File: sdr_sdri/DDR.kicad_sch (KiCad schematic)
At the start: 5 parts

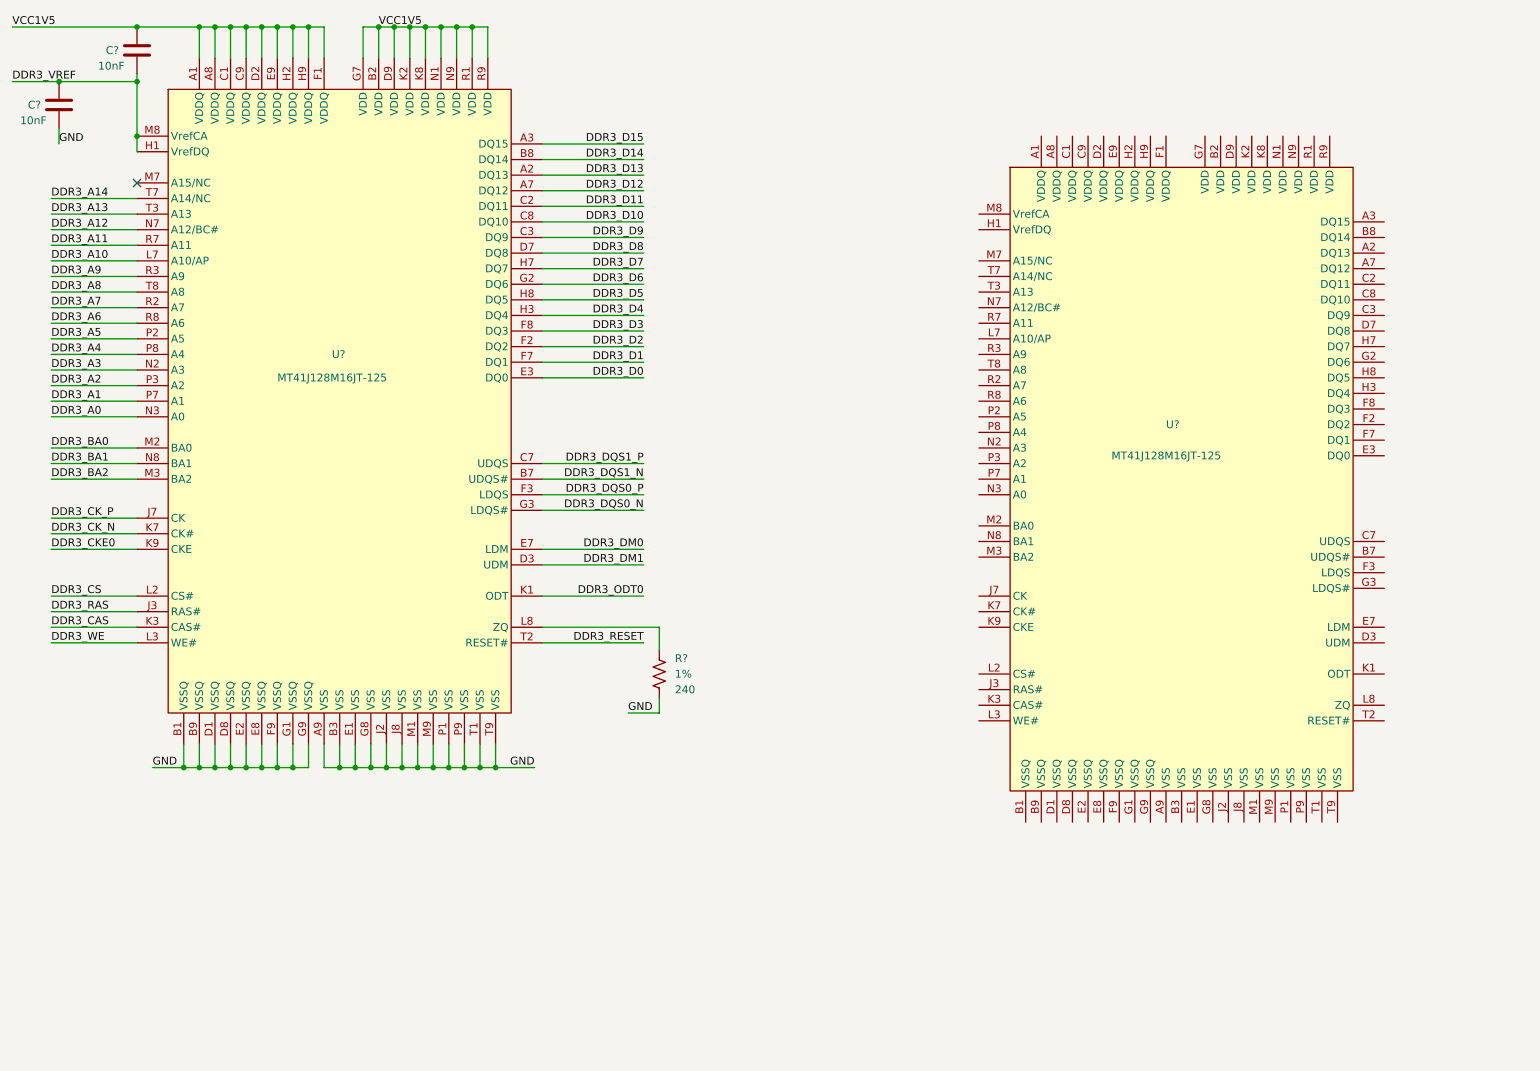
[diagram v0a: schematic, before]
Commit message: add ddr device
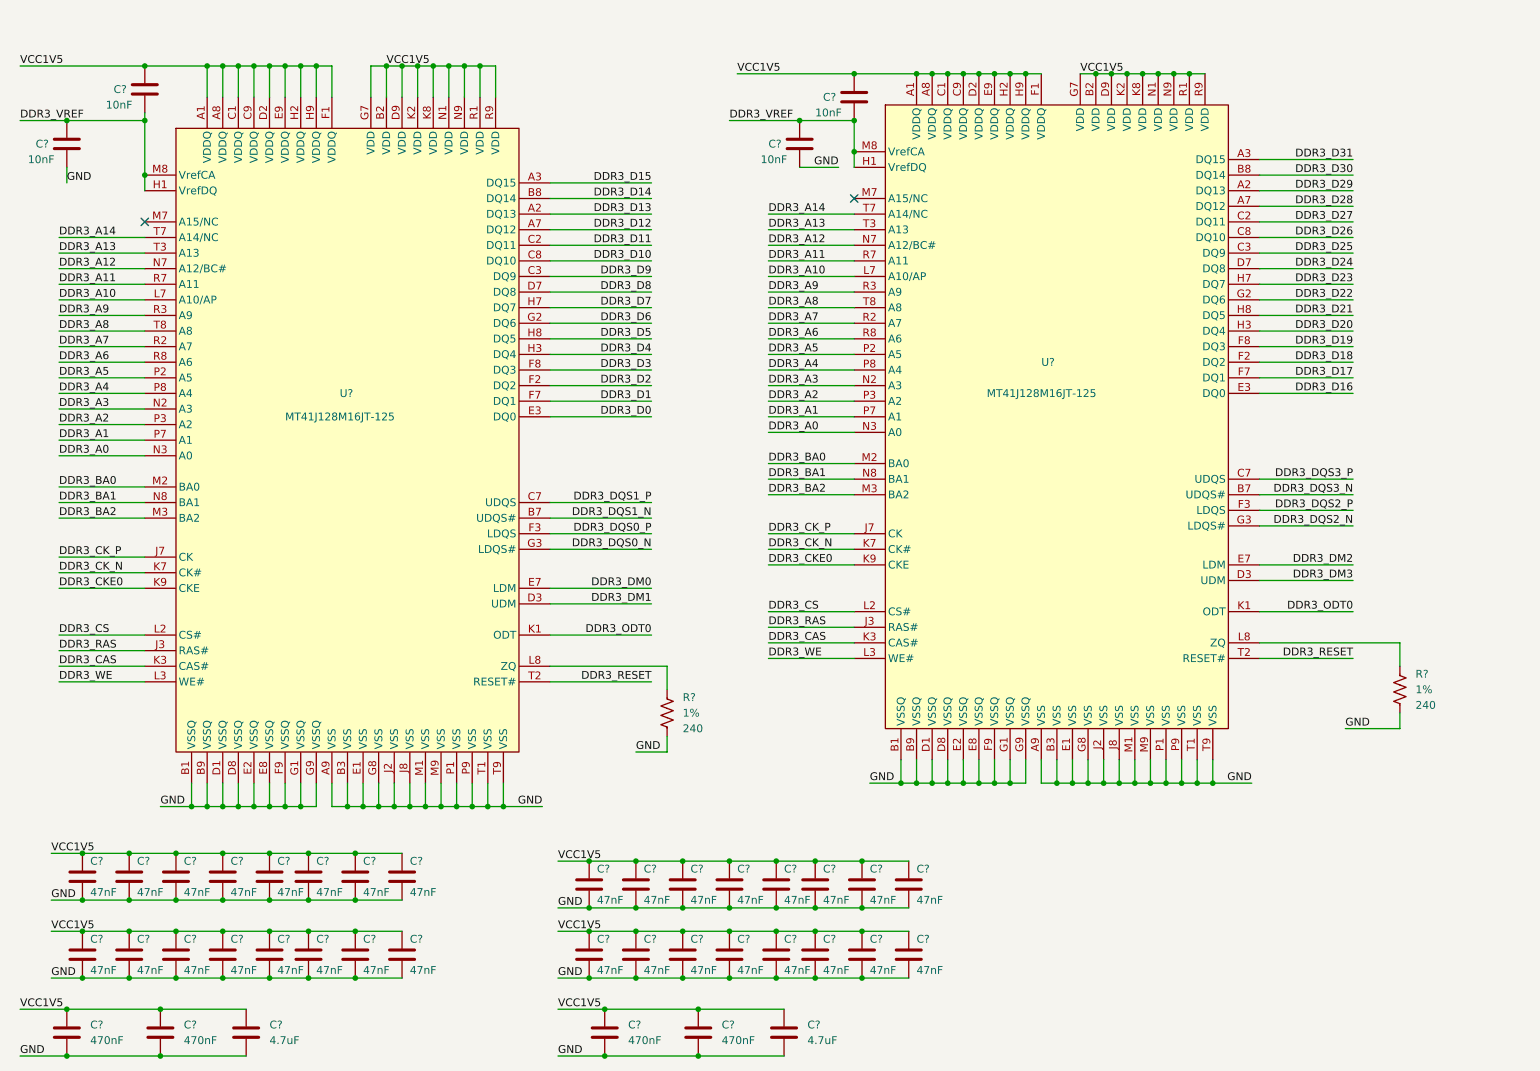
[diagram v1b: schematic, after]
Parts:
- added C? (x32): 47nF, symbol Device:C
- added C? (x2): 4.7uF, symbol Device:C
- added C? (x2): 10nF, symbol Device:C
- added C? (x4): 470nF, symbol Device:C
- added R?: 240, symbol Device:R_US
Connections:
- net DDR3_A0: now also U?.N3 (A0)
- net DDR3_A1: now also U?.P7 (A1)
- net DDR3_A10: now also U?.L7 (A10/AP)
- net DDR3_A11: now also U?.R7 (A11)
- net DDR3_A12: now also U?.N7 (A12/BC#)
- net DDR3_A13: now also U?.T3 (A13)
- net DDR3_A14: now also U?.T7 (A14/NC)
- net DDR3_A2: now also U?.P3 (A2)
- net DDR3_A3: now also U?.N2 (A3)
- net DDR3_A4: now also U?.P8 (A4)
- net DDR3_A5: now also U?.P2 (A5)
- net DDR3_A6: now also U?.R8 (A6)
- net DDR3_A7: now also U?.R2 (A7)
- net DDR3_A8: now also U?.T8 (A8)
- net DDR3_A9: now also U?.R3 (A9)
- net DDR3_BA0: now also U?.M2 (BA0)
- net DDR3_BA1: now also U?.N8 (BA1)
- net DDR3_BA2: now also U?.M3 (BA2)
- net DDR3_CAS: now also U?.K3 (CAS#)
- net DDR3_CKE0: now also U?.K9 (CKE)
- net DDR3_CK_N: now also U?.K7 (CK#)
- net DDR3_CK_P: now also U?.J7 (CK)
- net DDR3_CS: now also U?.L2 (CS#)
- net DDR3_ODT0: now also U?.K1 (ODT)
- net DDR3_RAS: now also U?.J3 (RAS#)
- net DDR3_RESET: now also U?.T2 (RESET#)
- net DDR3_VREF: now also U?.H1 (VrefDQ), U?.M8 (VrefCA), C?.1, C?.2
- net DDR3_WE: now also U?.L3 (WE#)
- net GND: now also U?.A9 (VSS), U?.B1 (VSSQ), U?.B3 (VSS), U?.B9 (VSSQ), U?.D1 (VSSQ), U?.D8 (VSSQ), U?.E1 (VSS), U?.E2 (VSSQ), U?.E8 (VSSQ), U?.F9 (VSSQ), U?.G1 (VSSQ), U?.G8 (VSS), U?.G9 (VSSQ), U?.J2 (VSS), U?.J8 (VSS), U?.M1 (VSS), U?.M9 (VSS), U?.P1 (VSS), U?.P9 (VSS), U?.T1 (VSS), U?.T9 (VSS), C?.2, C?.2, C?.2, C?.2, C?.2, C?.2, C?.2, C?.2, C?.2, C?.2, C?.2, C?.2, C?.2, C?.2, C?.2, C?.2, C?.2, C?.2, C?.2, C?.2, C?.2, C?.2, C?.2, C?.2, C?.2, C?.2, C?.2, C?.2, C?.2, C?.2, C?.2, C?.2, C?.2, C?.2, C?.2, C?.2, C?.2, C?.2, C?.2, R?.2
- net VCC1V5: now also U?.A1 (VDDQ), U?.A8 (VDDQ), U?.B2 (VDD), U?.C1 (VDDQ), U?.C9 (VDDQ), U?.D2 (VDDQ), U?.D9 (VDD), U?.E9 (VDDQ), U?.F1 (VDDQ), U?.G7 (VDD), U?.H2 (VDDQ), U?.H9 (VDDQ), U?.K2 (VDD), U?.K8 (VDD), U?.N1 (VDD), U?.N9 (VDD), U?.R1 (VDD), U?.R9 (VDD), C?.1, C?.1, C?.1, C?.1, C?.1, C?.1, C?.1, C?.1, C?.1, C?.1, C?.1, C?.1, C?.1, C?.1, C?.1, C?.1, C?.1, C?.1, C?.1, C?.1, C?.1, C?.1, C?.1, C?.1, C?.1, C?.1, C?.1, C?.1, C?.1, C?.1, C?.1, C?.1, C?.1, C?.1, C?.1, C?.1, C?.1, C?.1, C?.1
- net DDR3_D29: now reaches U?.A2 (DQ13)
- net DDR3_D31: now reaches U?.A3 (DQ15)
- net DDR3_D28: now reaches U?.A7 (DQ12)
- net DDR3_DQS3_N: now reaches U?.B7 (UDQS#)
- net DDR3_D30: now reaches U?.B8 (DQ14)
- net DDR3_D27: now reaches U?.C2 (DQ11)
- net DDR3_D25: now reaches U?.C3 (DQ9)
- net DDR3_DQS3_P: now reaches U?.C7 (UDQS)
- net DDR3_D26: now reaches U?.C8 (DQ10)
- net DDR3_DM3: now reaches U?.D3 (UDM)
- net DDR3_D24: now reaches U?.D7 (DQ8)
- net DDR3_D16: now reaches U?.E3 (DQ0)
- net DDR3_DM2: now reaches U?.E7 (LDM)
- net DDR3_D18: now reaches U?.F2 (DQ2)
- net DDR3_DQS2_P: now reaches U?.F3 (LDQS)
- net DDR3_D17: now reaches U?.F7 (DQ1)
- net DDR3_D19: now reaches U?.F8 (DQ3)
- net DDR3_D22: now reaches U?.G2 (DQ6)
- net DDR3_DQS2_N: now reaches U?.G3 (LDQS#)
- net DDR3_D20: now reaches U?.H3 (DQ4)
- net DDR3_D23: now reaches U?.H7 (DQ7)
- net DDR3_D21: now reaches U?.H8 (DQ5)
- net at U?.L8 (ZQ): now also R?.1
- no-connect marks 1 -> 2
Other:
- moved on the sheet: C?, R?, U?

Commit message: add some connection to fpga ddr
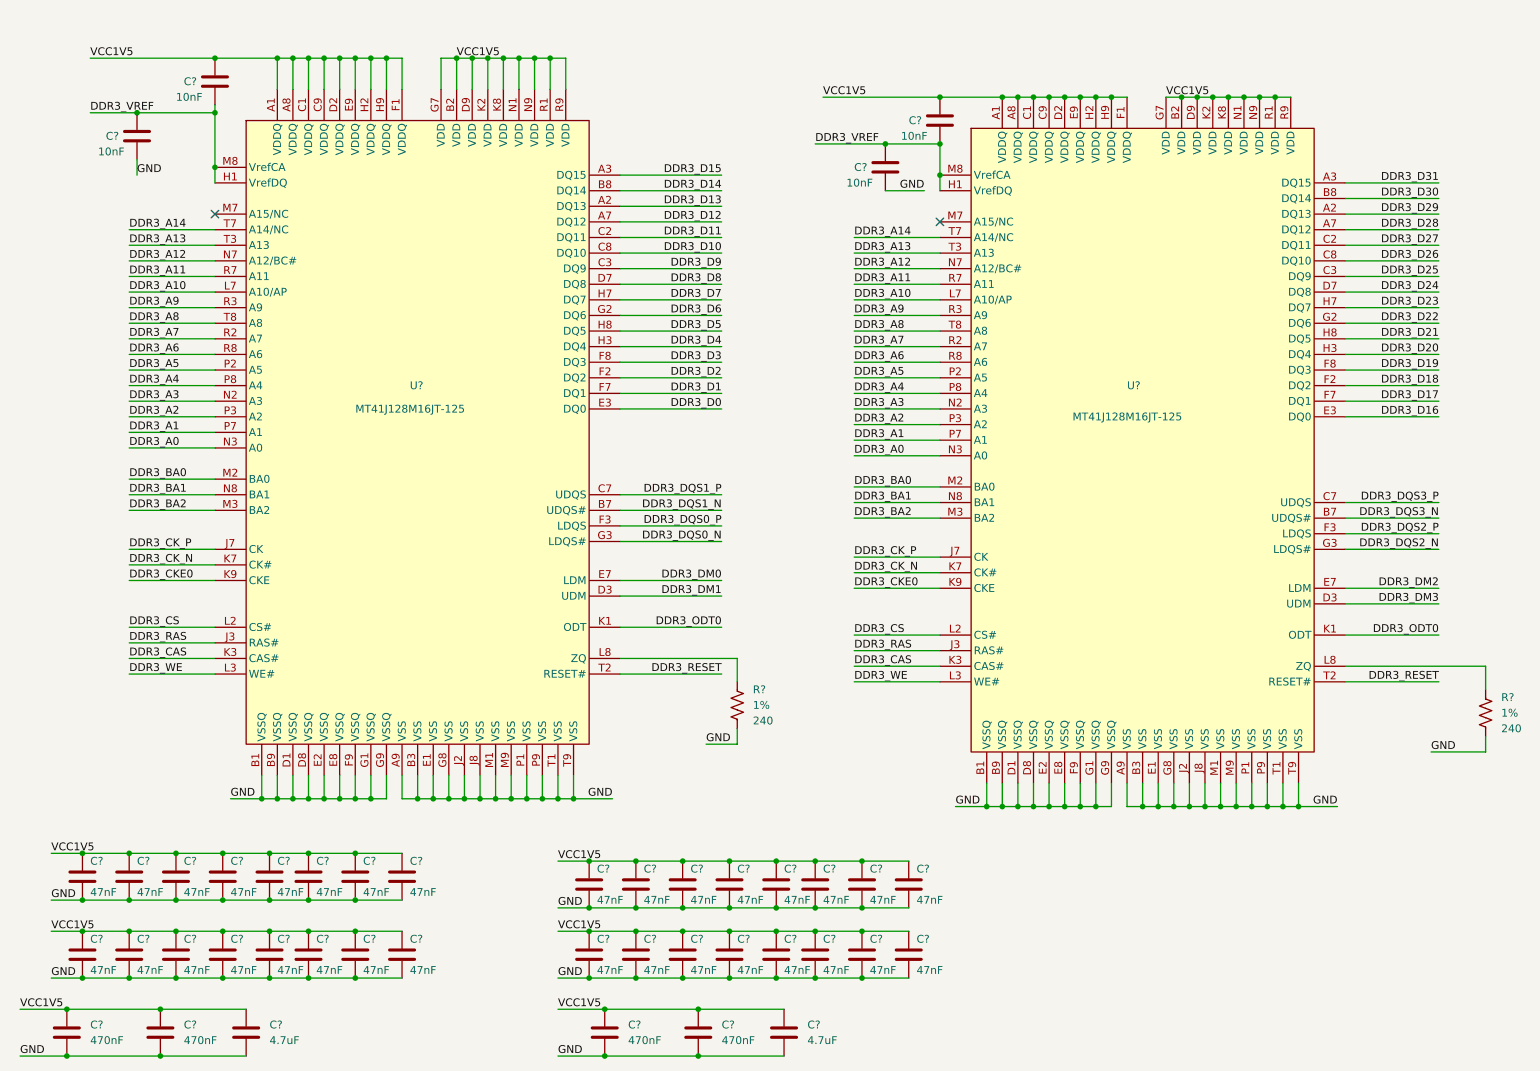
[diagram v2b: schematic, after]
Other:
- moved on the sheet: C?, R?, U?

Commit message: menambahkan connecsi k
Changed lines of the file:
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@@
+    (stroke (width 0) (type default) (color 0 0 0 0))
+  )
+  (wire (pts (xy 133.35 137.16) (xy 162.56 137.16))
     (stroke (width 0) (type default) (color 0 0 0 0))
   )
@@
     (stroke (width 0) (type default) (color 0 0 0 0))
   )
+  (wire (pts (xy 133.35 139.7) (xy 162.56 139.7))
+    (stroke (width 0) (type default) (color 0 0 0 0))
+  )
   (wire (pts (xy 60.96 170.18) (xy 67.31 170.18))
     (stroke (width 0) (type default) (color 0 0 0 0))
@@
     (stroke (width 0) (type default) (color 0 0 0 0))
   )
+  (wire (pts (xy 133.35 142.24) (xy 162.56 142.24))
+    (stroke (width 0) (type default) (color 0 0 0 0))
+  )
   (wire (pts (xy 38.1 73.66) (xy 52.07 73.66))
     (stroke (width 0) (type default) (color 0 0 0 0))
@@
     (effects (font (size 1.27 1.27)) (justify left bottom))
   )
+  (label "DDR_CKE" (at 133.35 142.24 0)
+    (effects (font (size 1.27 1.27)) (justify left bottom))
+  )
   (label "DDR3_A0" (at 156.21 85.09 0)
     (effects (font (size 1.27 1.27)) (justify left bottom))
@@
     (effects (font (size 1.27 1.27)) (justify left bottom))
   )
+  (label "DDR3_CK_N" (at 162.56 137.16 180)
+    (effects (font (size 1.27 1.27)) (justify right bottom))
+  )
   (label "DDR3_CK_N" (at 38.1 102.87 0)
     (effects (font (size 1.27 1.27)) (justify left bottom))
@@
     (effects (font (size 1.27 1.27)) (justify right bottom))
   )
+  (label "DDR3_CKE0" (at 162.56 142.24 180)
+    (effects (font (size 1.27 1.27)) (justify right bottom))
+  )
   (label "GND" (at 25.4 157.48 0)
     (effects (font (size 1.27 1.27)) (justify left bottom))
@@
     (effects (font (size 1.27 1.27)) (justify right bottom))
   )
+  (label "DDR_CKN" (at 133.35 137.16 0)
+    (effects (font (size 1.27 1.27)) (justify left bottom))
+  )
   (label "DDR3_D25" (at 251.46 55.88 180)
     (effects (font (size 1.27 1.27)) (justify right bottom))
@@
     (effects (font (size 1.27 1.27)) (justify right bottom))
   )
+  (label "DDR_CLKP" (at 133.35 139.7 0)
+    (effects (font (size 1.27 1.27)) (justify left bottom))
+  )
   (label "DDR3_D19" (at 251.46 71.12 180)
     (effects (font (size 1.27 1.27)) (justify right bottom))
@@
     (effects (font (size 1.27 1.27)) (justify left bottom))
   )
+  (label "DDR3_CK_P" (at 162.56 139.7 180)
+    (effects (font (size 1.27 1.27)) (justify right bottom))
+  )
   (label "DDR3_A9" (at 38.1 60.96 0)
